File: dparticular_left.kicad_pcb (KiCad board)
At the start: 2 copper layers, 185.7 x 157.2 mm, 48 parts, among them J2 USB from outside, J3 To Right Hand, J4 Jumper to Teensy USB, SW1:6 Key_Scrl, SW1:7 Key_Paus, SW2:1 Key_ESC, SW2:2 Key_F1, SW2:3 Key_F2, SW2:4 Key_F3, SW2:5 Key_F4, SW2:6 Key_F5, SW2:7 Key_F6, SW3:1 Key_Home, SW3:2 Key_End, SW3:3 Key_Tilde, SW3:4 Key_1, SW3:5 Key_2, SW3:6 Key_3, SW3:7 Key_4, SW3:8 Key_5, SW4:2 Key_PgUp, SW4:3 Key_Tab, SW4:4 Key_Q, SW4:5 Key_W, SW4:6 Key_E, SW4:7 Key_R, SW4:8 Key_T, SW5:2 Key_PgDn, SW5:3 Key_Caps, SW5:4 Key_A, SW5:5 Key_S, SW5:6 Key_D, SW5:7 Key_F, SW5:8 Key_G, SW6:3 Key_LShft, SW6:4 Key_Z, SW6:5 Key_X, SW6:6 Key_C, SW6:7 Key_V, SW6:8 Key_B, SW7:3 Key_LCtrl, SW7:4 Key_Fn, SW7:5 Key_LWin, SW7:6 Key_LAlt, SW7:8 Key_LSpc, U2 TEENSY2.0

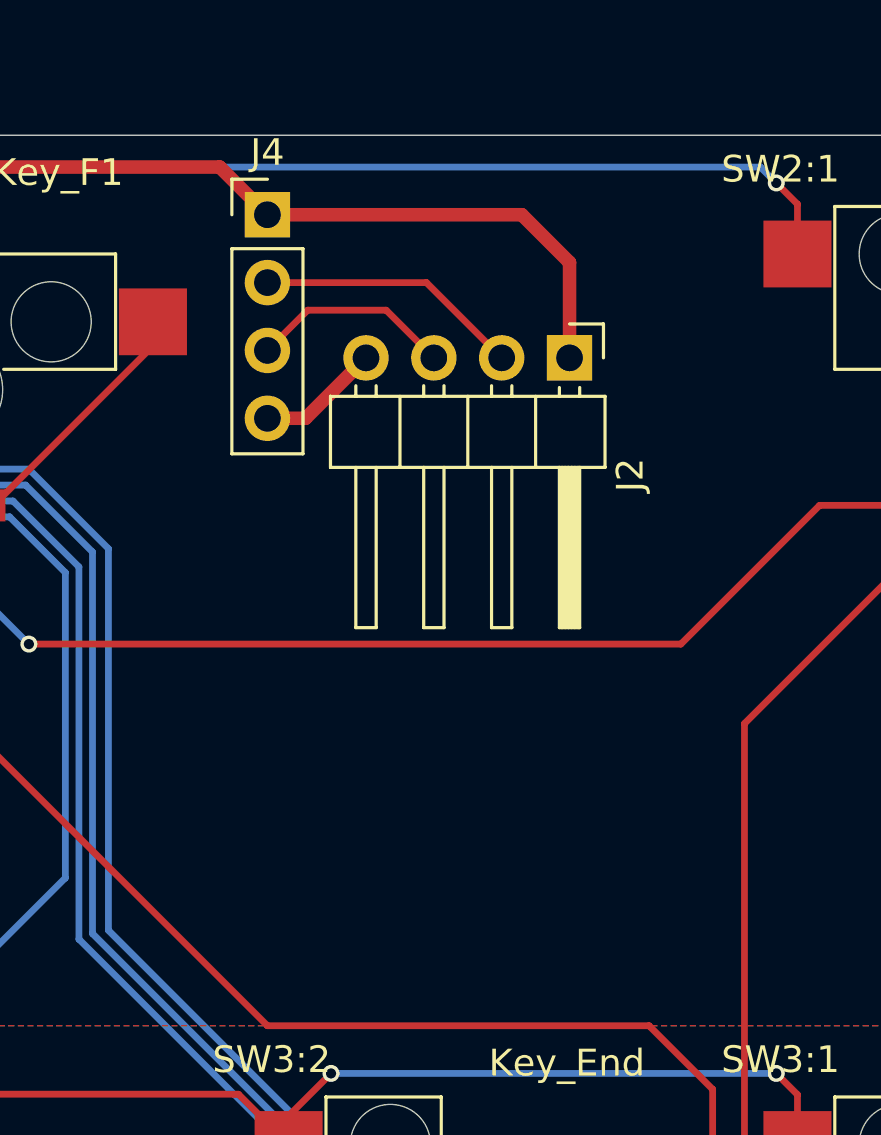
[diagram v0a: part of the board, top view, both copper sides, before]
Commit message: Left PCB: Mounting holes for USB strain relief zip ties
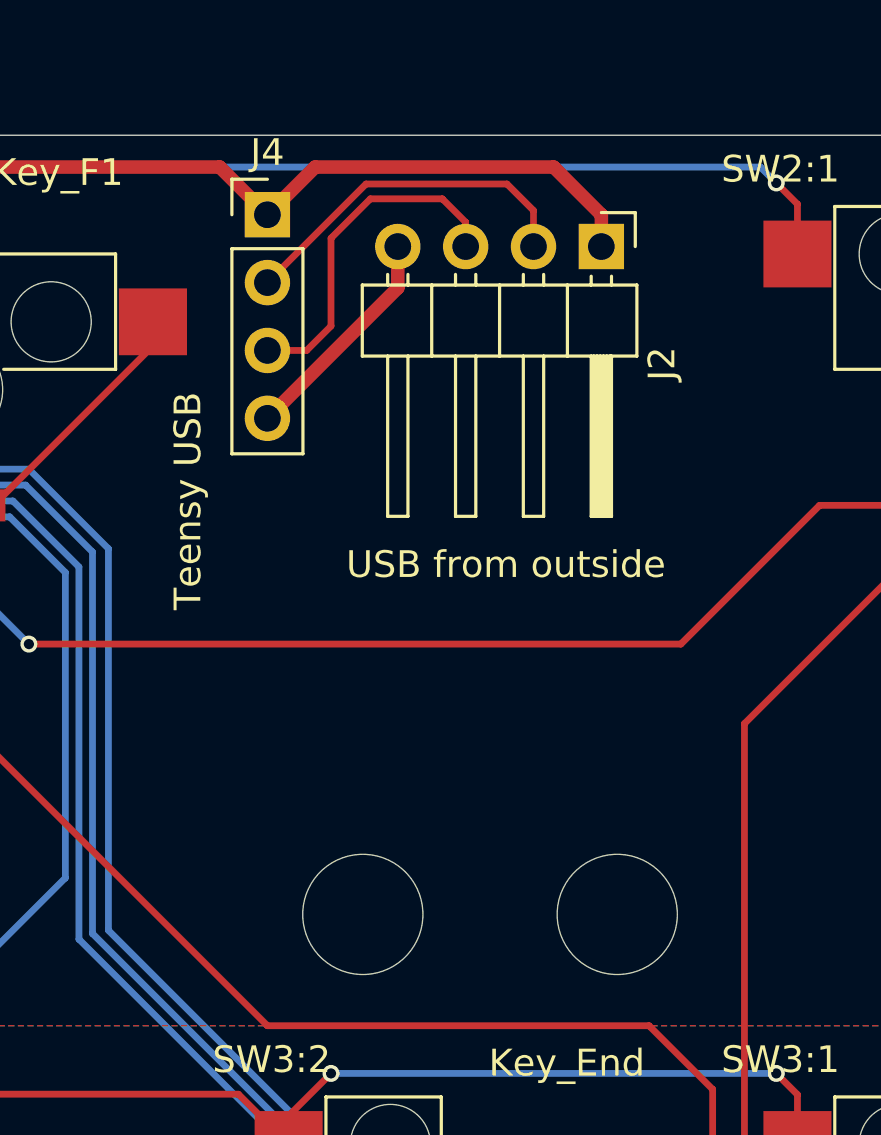
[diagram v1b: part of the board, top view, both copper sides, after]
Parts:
- added H1: USB Strain L, MountingHole:MountingHole_4.5mm, F.Cu at (172.6, 76.8)
- added H2: USB Strain R, MountingHole:MountingHole_4.5mm, F.Cu at (182.2, 76.8)
- J4: value Jumper to Teensy USB -> Teensy USB
- moved J2 4.33 mm to (181.6, 51.8)
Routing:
- net /USB_DP: track 7.60 -> 13.0 mm
- net GND: track 4.63 -> 8.45 mm
- net /USB_DN: track 9.94 -> 13.3 mm
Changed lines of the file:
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@@
     (thickness 1.6)
     (drawings 51)
-    (tracks 757)
+    (tracks 764)
     (zones 0)
-    (modules 48)
+    (modules 50)
     (nets 70)
   )
@@
     (add_net "Net-(U2-Pad20)")
   )
+  (module MountingHole:MountingHole_4.5mm (layer F.Cu)
+    (at 182.165504 76.79528)
+    (descr "Mounting Hole 4.5mm, no annular")
+    (tags "mounting hole 4.5mm no annular")
+    (attr virtual)
+    (fp_text reference H2 (at 0 -5.5) (layer F.Fab)
+      (effects (font (size 1 1) (thickness 0.15)))
+    )
+    (fp_text value "USB Strain R" (at 6.548432 -2.381248 270) (layer F.Fab)
+      (effects (font (size 1 1) (thickness 0.15)))
+    )
+    (fp_text user %R (at 0.3 0) (layer F.Fab)
+      (effects (font (size 1 1) (thickness 0.15)))
+    )
+    (fp_circle (center 0 0) (end 4.5 0) (layer Cmts.User) (width 0.15))
+    (fp_circle (center 0 0) (end 4.75 0) (layer F.CrtYd) (width 0.05))
+    (pad 1 np_thru_hole circle (at 0 0) (size 4.5 4.5) (drill 4.5) (layers *.Cu *.Mask))
+  )
+  (module MountingHole:MountingHole_4.5mm (layer F.Cu)
+    (at 172.640512 76.79528)
+    (descr "Mounting Hole 4.5mm, no annular")
+    (tags "mounting hole 4.5mm no annular")
+    (attr virtual)
+    (fp_text reference H1 (at 0 -5.5) (layer F.Fab)
+      (effects (font (size 1 1) (thickness 0.15)))
+    )
+    (fp_text value "USB Strain L" (at -5.95312 -4.167184 270) (layer F.Fab)
+      (effects (font (size 1 1) (thickness 0.15)))
+    )
+    (fp_text user %R (at 0.3 0) (layer F.Fab)
+      (effects (font (size 1 1) (thickness 0.15)))
+    )
+    (fp_circle (center 0 0) (end 4.5 0) (layer Cmts.User) (width 0.15))
+    (fp_circle (center 0 0) (end 4.75 0) (layer F.CrtYd) (width 0.05))
+    (pad 1 np_thru_hole circle (at 0 0) (size 4.5 4.5) (drill 4.5) (layers *.Cu *.Mask))
+  )
   (module dparticular:MX_W_DIODE (layer F.Cu)
     (at 157.1625 57.15)
@@
       (effects (font (size 1 1) (thickness 0.15)))
     )
-    (fp_text value "Jumper to Teensy USB" (at 0 9.95) (layer F.Fab)
+    (fp_text value "Teensy USB" (at -2.97656 10.715616 90) (layer F.SilkS)
       (effects (font (size 1 1) (thickness 0.15)))
     )
@@
   )
   (module Connector_PinHeader_2.54mm:PinHeader_1x04_P2.54mm_Horizontal (layer F.Cu)
-    (at 180.379568 55.95936 270)
+    (at 181.570192 51.792176 270)
     (descr "Through hole angled pin header, 1x04, 2.54mm pitch, 6mm pin length, single row")
     (tags "Through hole angled pin header THT 1x04 2.54mm single row")
@@
       (effects (font (size 1 1) (thickness 0.15)))
     )
-    (fp_text value "USB from outside" (at 4.385 9.89 90) (layer F.Fab)
+    (fp_text value "USB from outside" (at 11.90624 3.571872 180) (layer F.SilkS)
       (effects (font (size 1 1) (thickness 0.15)))
     )
@@
   (segment (start 167.282722 48.815634) (end 169.06864 50.601552) (width 0.508) (layer F.Cu) (net 1))
   (segment (start 126.444384 48.815634) (end 167.282722 48.815634) (width 0.508) (layer F.Cu) (net 1))
-  (segment (start 180.379568 55.95936) (end 180.379568 52.387751) (width 0.508) (layer F.Cu) (net 1))
-  (segment (start 178.593369 50.601552) (end 169.06864 50.601552) (width 0.508) (layer F.Cu) (net 1))
-  (segment (start 180.379568 52.387751) (end 178.593369 50.601552) (width 0.508) (layer F.Cu) (net 1))
   (segment (start 59.53125 78.58125) (end 64.29375 73.81875) (width 0.508) (layer B.Cu) (net 1))
   (segment (start 50.00625 78.58125) (end 59.53125 78.58125) (width 0.508) (layer B.Cu) (net 1))
@@
   (segment (start 44.648443 67.86565) (end 44.648443 73.223443) (width 0.508) (layer B.Cu) (net 1))
   (segment (start 51.196886 35.123435) (end 51.196886 61.317207) (width 0.508) (layer B.Cu) (net 1))
-  (segment (start 175.02176 53.141552) (end 177.839568 55.95936) (width 0.254) (layer F.Cu) (net 2))
-  (segment (start 169.06864 53.141552) (end 175.02176 53.141552) (width 0.254) (layer F.Cu) (net 2))
-  (segment (start 169.06864 55.681552) (end 170.576741 54.173451) (width 0.254) (layer F.Cu) (net 3))
-  (segment (start 173.513659 54.173451) (end 175.299568 55.95936) (width 0.254) (layer F.Cu) (net 3))
-  (segment (start 170.576741 54.173451) (end 173.513659 54.173451) (width 0.254) (layer F.Cu) (net 3))
-  (segment (start 170.497376 58.221552) (end 172.759568 55.95936) (width 0.508) (layer F.Cu) (net 4))
-  (segment (start 169.06864 58.221552) (end 170.497376 58.221552) (width 0.508) (layer F.Cu) (net 4))
+  (segment (start 169.06864 50.601552) (end 170.854576 48.815616) (width 0.508) (layer F.Cu) (net 1))
+  (segment (start 170.854576 48.815616) (end 179.784256 48.815616) (width 0.508) (layer F.Cu) (net 1))
+  (segment (start 181.570192 50.601552) (end 181.570192 51.792176) (width 0.508) (layer F.Cu) (net 1))
+  (segment (start 179.784256 48.815616) (end 181.570192 50.601552) (width 0.508) (layer F.Cu) (net 1))
+  (segment (start 179.030192 50.4428) (end 179.030192 51.792176) (width 0.254) (layer F.Cu) (net 2))
+  (segment (start 178.038018 49.450626) (end 179.030192 50.4428) (width 0.254) (layer F.Cu) (net 2))
+  (segment (start 169.06864 53.141552) (end 172.759566 49.450626) (width 0.254) (layer F.Cu) (net 2))
+  (segment (start 172.759566 49.450626) (end 178.038018 49.450626) (width 0.254) (layer F.Cu) (net 2))
+  (segment (start 169.06864 55.681552) (end 170.537072 55.681552) (width 0.254) (layer F.Cu) (net 3))
+  (segment (start 171.449888 54.768736) (end 171.449888 51.478738) (width 0.254) (layer F.Cu) (net 3))
+  (segment (start 170.537072 55.681552) (end 171.449888 54.768736) (width 0.254) (layer F.Cu) (net 3))
+  (segment (start 171.449888 51.478738) (end 172.922386 50.00624) (width 0.254) (layer F.Cu) (net 3))
+  (segment (start 172.922386 50.00624) (end 175.617072 50.00624) (width 0.254) (layer F.Cu) (net 3))
+  (segment (start 176.490192 50.87936) (end 176.490192 51.792176) (width 0.254) (layer F.Cu) (net 3))
+  (segment (start 175.617072 50.00624) (end 176.490192 50.87936) (width 0.254) (layer F.Cu) (net 3))
+  (segment (start 173.950192 53.34) (end 173.950192 51.792176) (width 0.508) (layer F.Cu) (net 4))
+  (segment (start 169.06864 58.221552) (end 173.950192 53.34) (width 0.508) (layer F.Cu) (net 4))
   (segment (start 54.45125 76.04125) (end 56.67375 73.81875) (width 0.254) (layer B.Cu) (net 5))
   (segment (start 50.00625 76.04125) (end 54.45125 76.04125) (width 0.254) (layer B.Cu) (net 5))

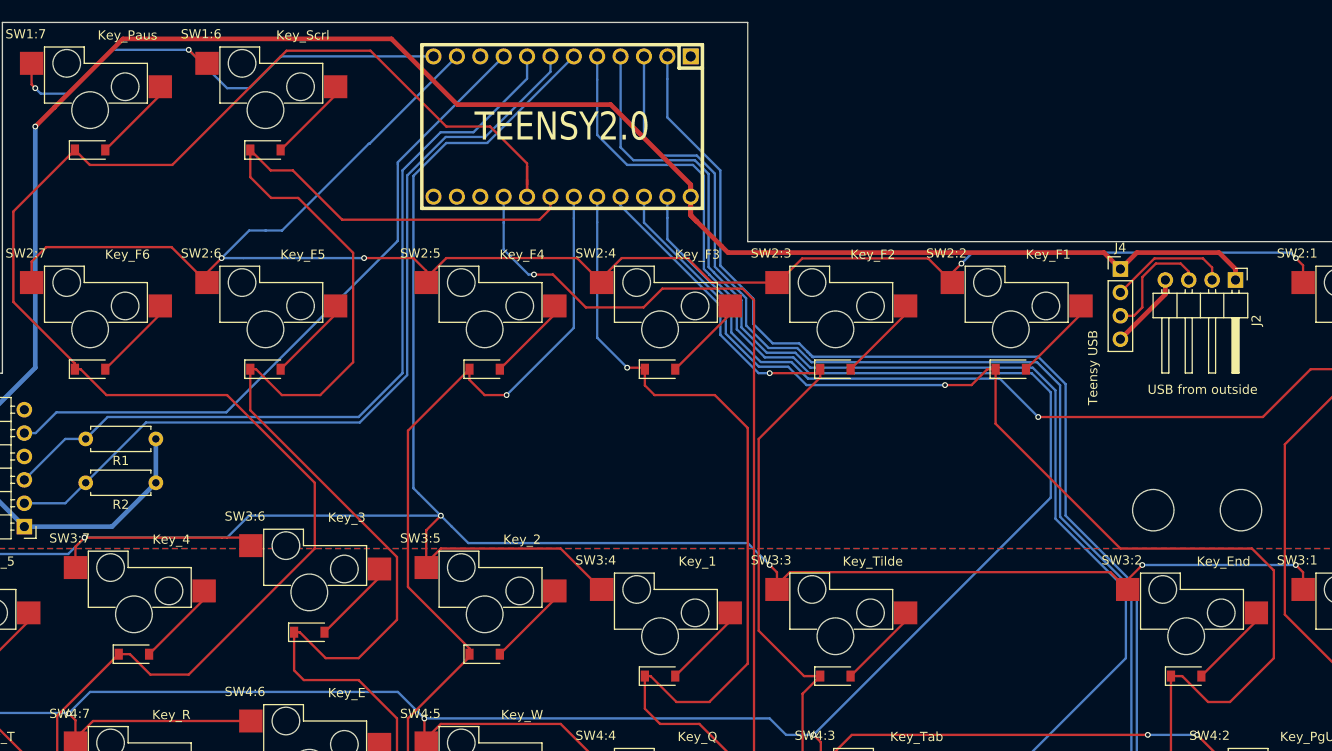
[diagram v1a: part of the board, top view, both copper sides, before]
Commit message: Left Hand PCB: Reset switch for Teensy 2.0
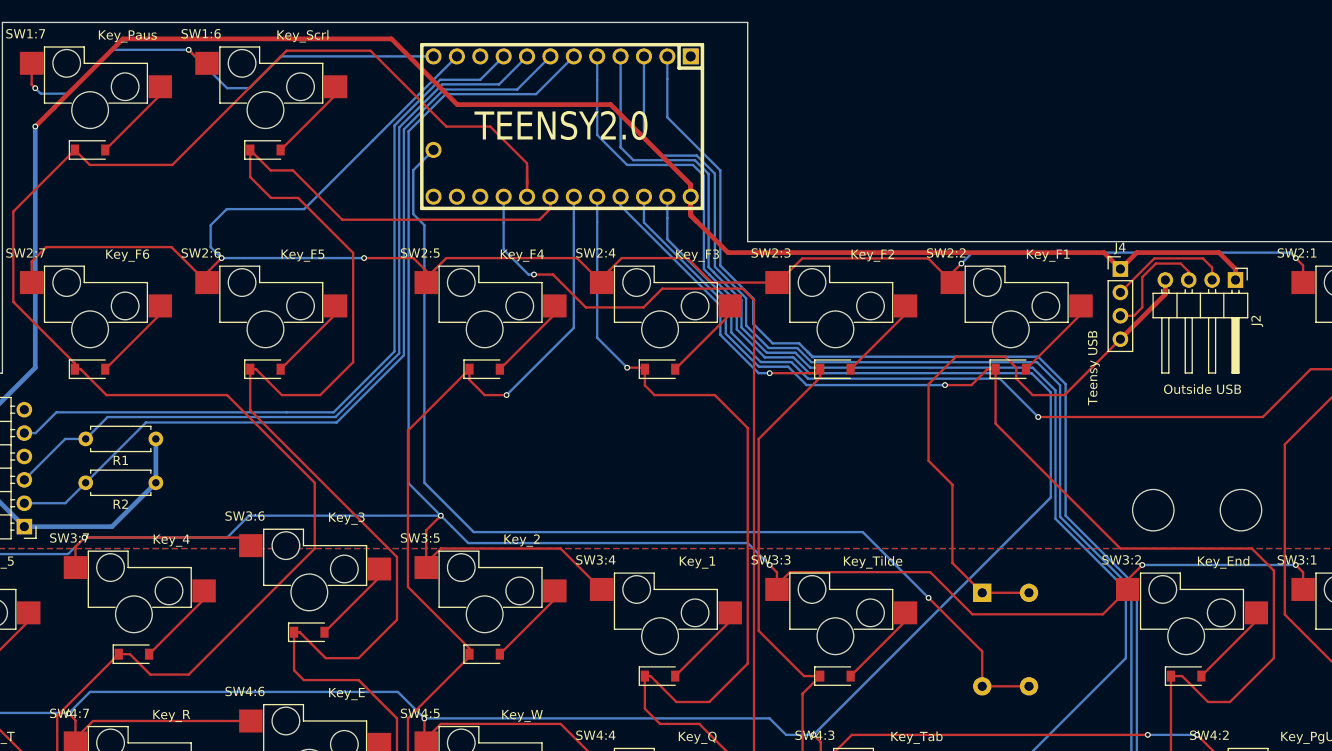
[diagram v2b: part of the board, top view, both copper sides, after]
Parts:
- added SW1: Reset, dparticular:JB15HAP-2A, B.Cu at (156.6, 90.8)
- J2: value USB from outside -> Outside USB
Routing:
- net Net-(SW1-Pad2): track 0.00 -> 114.6 mm, vias 0 -> 1
- net GND: track 8.45 -> 65.6 mm
- net /LED_D: track 74.0 -> 83.4 mm
- net /ROW3: track 277.5 -> 283.3 mm
- net /ROW2: track 192.4 -> 196.2 mm
- net /SCL: track 90.9 -> 91.6 mm

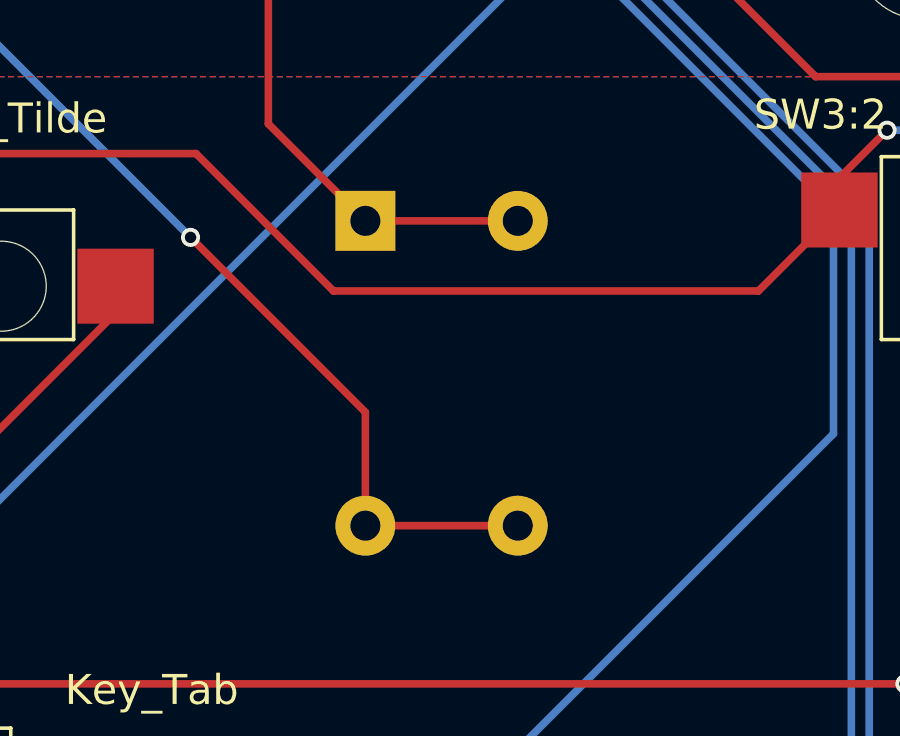
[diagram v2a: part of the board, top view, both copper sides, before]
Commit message: Left Hand PCB: Shorter switch, properly positioned
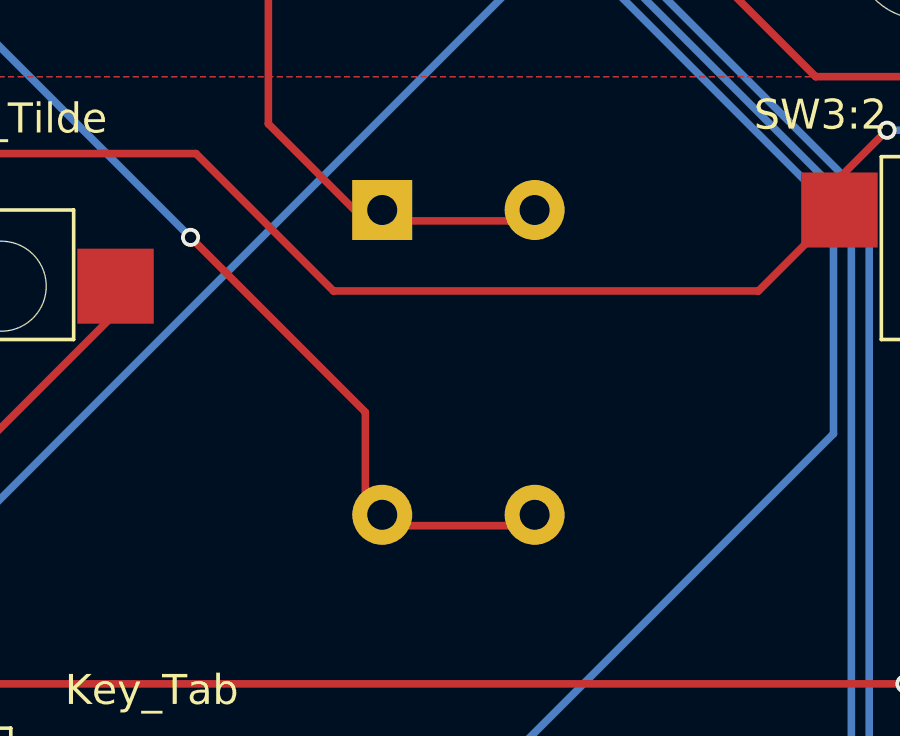
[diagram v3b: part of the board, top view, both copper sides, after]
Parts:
- SW1: footprint dparticular:JB15HAP-2A -> dparticular:JB15KP-2A
- moved SW1 0.67 mm to (157.2, 90.5)
